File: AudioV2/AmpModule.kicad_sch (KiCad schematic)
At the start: 26 parts, among them J701 AMP_IN L/R, J702 AMP_OUT L/R, J703 +12V / A_GND / -12V

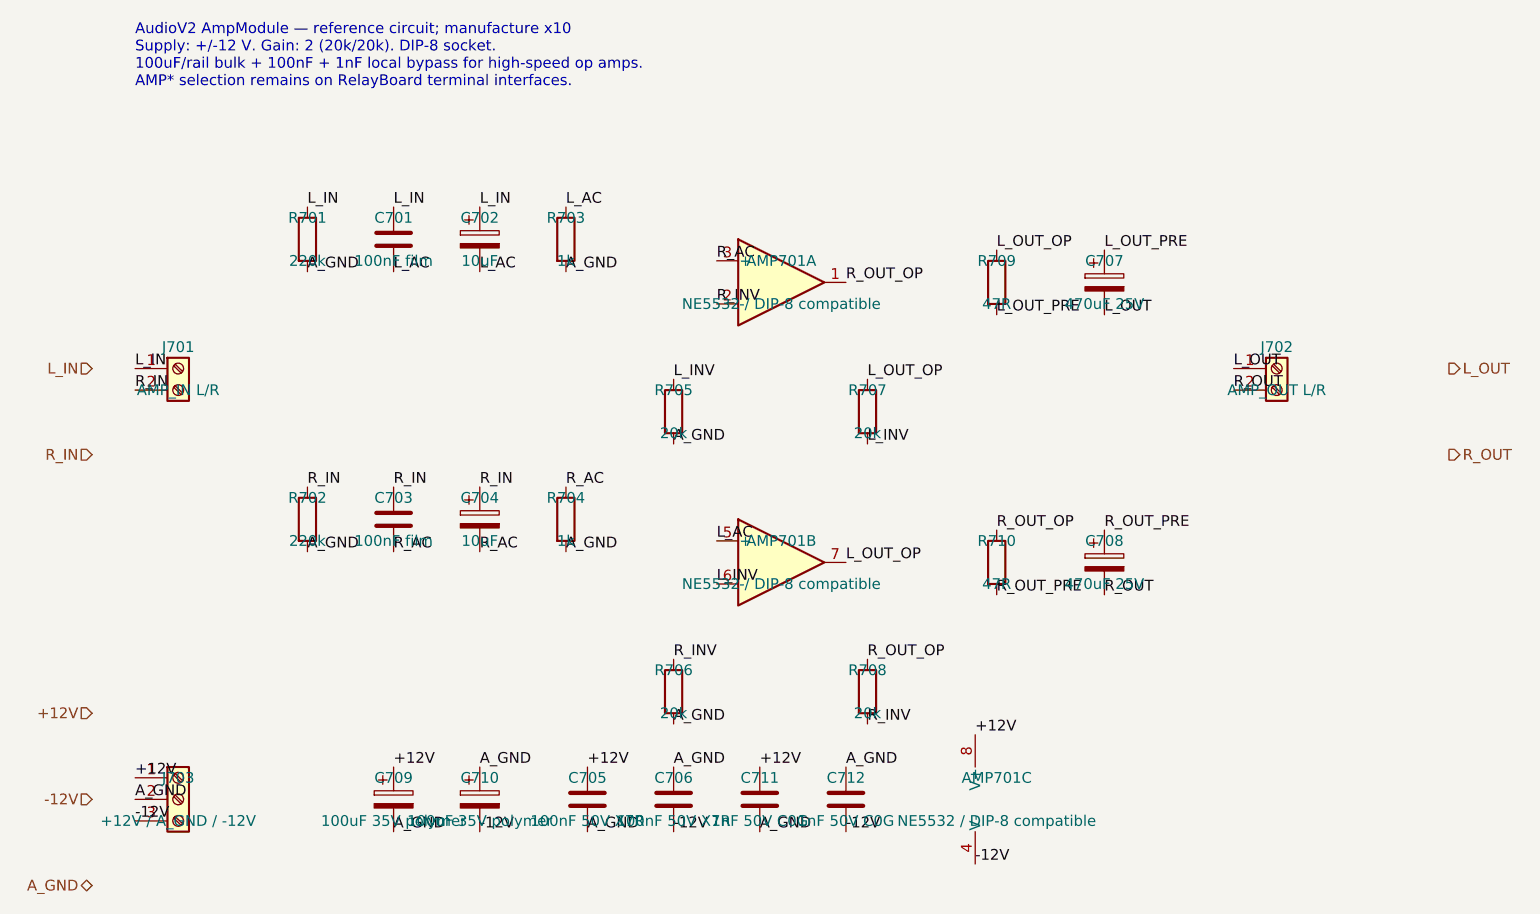
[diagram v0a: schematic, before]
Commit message: AudioV2: 全シートを再アノテーション、参照変更を生成スクリプトと文書へ反映
KiCad で再アノテーションし、参照の重複と未付番を解消（計58件が変更）。

- ControlPanel の C201-C208 が PowerModule と重複していたため 5xx 台へ移動
- 未付番だった J_OLED を J_OLED501 に
- RelayBoard で U301(MCP23017) と U302(ULN2803A SET側) が入れ替わり
  → MCP23017 は U302、SET側 ULN が U301。接続トポロジは変更なし
- OutputStage が 6xx 台へ、AmpModule の C7xx/R7xx が L/R 対称に整列
- これにより netlist 出力時の「注釈のエラー」警告が解消

wire_circuit_design.py は旧参照をハードコードしており、再生成すると
アノテーションが巻き戻る状態だった。生成関数の行範囲でスコープを切って
86箇所を同時置換（U1 が PowerModule と ControlPanel で別部品のため）。
サンドボックスで再生成して実図と突き合わせ、AmpModule / ControlPanel /
RelayBoard / AudioV2Case は参照・値とも完全一致することを確認。
変更前後どちらの生成物も ERC 80件で、本修正は ERC 中立。

文書側も 7ファイル52箇所を更新。PARTS.md の「R705-708」等の範囲表記は
振り直し後に連番でなくなるため書き直し、OutputStage の表は SW_SP3T×2 の
実ピン（ネット名で照合）に合わせた。DECISIONS.md の D1/D2/D3 は決定ID、
旧 Audio/ SW101 参照は別プロジェクト指定のため意図的に据え置き。

既知の未同期: PowerModule はスクリプトが一世代古い（USB-C+CH224 の PD
前段を生成するが実図は PD モジュール外付け）。参照対応が一意に決まらない
ため F1→F201 / U1→U201 / U3→U202 / J202→J201 のみ修正し、コンデンサ群は
未着手。OutputStage の J_RAIL601 も生成対象外。

ERC は実図 54件で変化なし。

Co-Authored-By: Claude Opus 5 <noreply@anthropic.com>
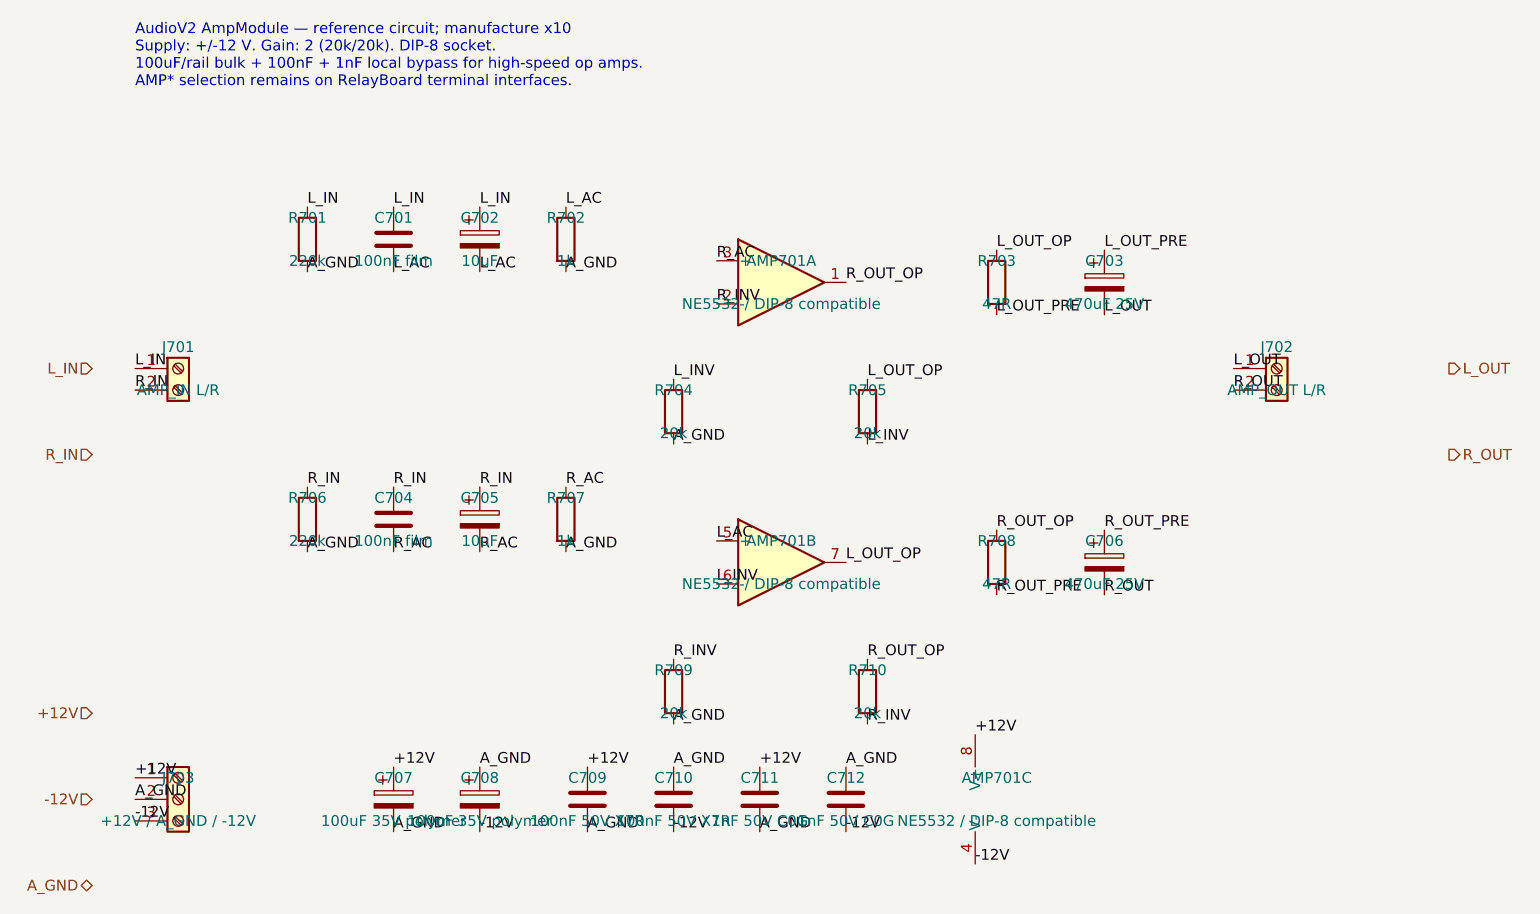
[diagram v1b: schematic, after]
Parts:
- renumbered C707 to C703, C703 to C704, C704 to C705, C708 to C706, C709 to C707, C710 to C708, C705 to C709, C706 to C710, R703 to R702, R709 to R703, R705 to R704, R707 to R705, R702 to R706, R704 to R707, R710 to R708, R706 to R709, R708 to R710
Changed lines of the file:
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@@
 		(dnp no)
 		(fields_autoplaced yes)
-		(property "Reference" "R707"
+		(property "Reference" "R705"
 			(at 111.76 63.5 0)
 			(show_name no)
@@
 			(project "AudioV2Case"
 				(path "/a1000001-0001-4001-8001-000000000001/a1000008-0008-4008-8008-000000000008"
-					(reference "R707")
+					(reference "R705")
 					(unit 1)
 				)
@@
 		(dnp no)
 		(fields_autoplaced yes)
-		(property "Reference" "C709"
+		(property "Reference" "C707"
 			(at 55.88 109.22 0)
 			(show_name no)
@@
 			(project "AudioV2Case"
 				(path "/a1000001-0001-4001-8001-000000000001/a1000008-0008-4008-8008-000000000008"
-					(reference "C709")
+					(reference "C707")
 					(unit 1)
 				)
@@
 		(dnp no)
 		(fields_autoplaced yes)
-		(property "Reference" "R702"
+		(property "Reference" "R706"
 			(at 45.72 76.2 0)
 			(show_name no)
@@
 			(project "AudioV2Case"
 				(path "/a1000001-0001-4001-8001-000000000001/a1000008-0008-4008-8008-000000000008"
-					(reference "R702")
+					(reference "R706")
 					(unit 1)
 				)
@@
 		(dnp no)
 		(fields_autoplaced yes)
-		(property "Reference" "C708"
+		(property "Reference" "C706"
 			(at 139.7 81.28 0)
 			(show_name no)
@@
 			(project "AudioV2Case"
 				(path "/a1000001-0001-4001-8001-000000000001/a1000008-0008-4008-8008-000000000008"
-					(reference "C708")
+					(reference "C706")
 					(unit 1)
 				)
@@
 		(dnp no)
 		(fields_autoplaced yes)
-		(property "Reference" "C704"
+		(property "Reference" "C705"
 			(at 66.04 76.2 0)
 			(show_name no)
@@
 			(project "AudioV2Case"
 				(path "/a1000001-0001-4001-8001-000000000001/a1000008-0008-4008-8008-000000000008"
-					(reference "C704")
+					(reference "C705")
 					(unit 1)
 				)
@@
 		(dnp no)
 		(fields_autoplaced yes)
-		(property "Reference" "R703"
+		(property "Reference" "R702"
 			(at 76.2 43.18 0)
 			(show_name no)
@@
 			(project "AudioV2Case"
 				(path "/a1000001-0001-4001-8001-000000000001/a1000008-0008-4008-8008-000000000008"
-					(reference "R703")
+					(reference "R702")
 					(unit 1)
 				)
@@
 		(dnp no)
 		(fields_autoplaced yes)
-		(property "Reference" "C703"
+		(property "Reference" "C704"
 			(at 55.88 76.2 0)
 			(show_name no)
@@
 			(project "AudioV2Case"
 				(path "/a1000001-0001-4001-8001-000000000001/a1000008-0008-4008-8008-000000000008"
-					(reference "C703")
+					(reference "C704")
 					(unit 1)
 				)
@@
 		(dnp no)
 		(fields_autoplaced yes)
-		(property "Reference" "R708"
+		(property "Reference" "R710"
 			(at 111.76 96.52 0)
 			(show_name no)
@@
 			(project "AudioV2Case"
 				(path "/a1000001-0001-4001-8001-000000000001/a1000008-0008-4008-8008-000000000008"
-					(reference "R708")
+					(reference "R710")
 					(unit 1)
 				)
@@
 		(dnp no)
 		(fields_autoplaced yes)
-		(property "Reference" "C705"
+		(property "Reference" "C709"
 			(at 78.74 109.22 0)
 			(show_name no)
@@
 			(project "AudioV2Case"
 				(path "/a1000001-0001-4001-8001-000000000001/a1000008-0008-4008-8008-000000000008"
-					(reference "C705")
+					(reference "C709")
 					(unit 1)
 				)
@@
 		(dnp no)
 		(fields_autoplaced yes)
-		(property "Reference" "R709"
+		(property "Reference" "R703"
 			(at 127 48.26 0)
 			(show_name no)
@@
 			(project "AudioV2Case"
 				(path "/a1000001-0001-4001-8001-000000000001/a1000008-0008-4008-8008-000000000008"
-					(reference "R709")
+					(reference "R703")
 					(unit 1)
 				)
@@
 		(dnp no)
 		(fields_autoplaced yes)
-		(property "Reference" "C706"
+		(property "Reference" "C710"
 			(at 88.9 109.22 0)
 			(show_name no)
@@
 			(project "AudioV2Case"
 				(path "/a1000001-0001-4001-8001-000000000001/a1000008-0008-4008-8008-000000000008"
-					(reference "C706")
+					(reference "C710")
 					(unit 1)
 				)
@@
 		(dnp no)
 		(fields_autoplaced yes)
-		(property "Reference" "R706"
+		(property "Reference" "R709"
 			(at 88.9 96.52 0)
 			(show_name no)
@@
 			(project "AudioV2Case"
 				(path "/a1000001-0001-4001-8001-000000000001/a1000008-0008-4008-8008-000000000008"
-					(reference "R706")
+					(reference "R709")
 					(unit 1)
 				)
@@
 		(dnp no)
 		(fields_autoplaced yes)
-		(property "Reference" "C707"
+		(property "Reference" "C703"
 			(at 139.7 48.26 0)
 			(show_name no)
@@
 			(project "AudioV2Case"
 				(path "/a1000001-0001-4001-8001-000000000001/a1000008-0008-4008-8008-000000000008"
-					(reference "C707")
+					(reference "C703")
 					(unit 1)
 				)
@@
 		(dnp no)
 		(fields_autoplaced yes)
-		(property "Reference" "R704"
+		(property "Reference" "R707"
 			(at 76.2 76.2 0)
 			(show_name no)
@@
 			(project "AudioV2Case"
 				(path "/a1000001-0001-4001-8001-000000000001/a1000008-0008-4008-8008-000000000008"
-					(reference "R704")
+					(reference "R707")
 					(unit 1)
 				)
@@
 		(dnp no)
 		(fields_autoplaced yes)
-		(property "Reference" "R705"
+		(property "Reference" "R704"
 			(at 88.9 63.5 0)
 			(show_name no)
@@
 			(project "AudioV2Case"
 				(path "/a1000001-0001-4001-8001-000000000001/a1000008-0008-4008-8008-000000000008"
-					(reference "R705")
+					(reference "R704")
 					(unit 1)
 				)
@@
 		(dnp no)
 		(fields_autoplaced yes)
-		(property "Reference" "R710"
+		(property "Reference" "R708"
 			(at 127 81.28 0)
 			(show_name no)
@@
 			(project "AudioV2Case"
 				(path "/a1000001-0001-4001-8001-000000000001/a1000008-0008-4008-8008-000000000008"
-					(reference "R710")
+					(reference "R708")
 					(unit 1)
 				)
@@
 		(dnp no)
 		(fields_autoplaced yes)
-		(property "Reference" "C710"
+		(property "Reference" "C708"
 			(at 66.04 109.22 0)
 			(show_name no)
@@
 			(project "AudioV2Case"
 				(path "/a1000001-0001-4001-8001-000000000001/a1000008-0008-4008-8008-000000000008"
-					(reference "C710")
-					(unit 1)
-				)
+					(reference "C708")
+					(unit 1)
+				)
